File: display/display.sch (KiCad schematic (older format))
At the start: 11 parts

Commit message: More Display work
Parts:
- added C?: 100u, symbol Device:CP
- added C? (x3): 47n, symbol Device:C
- added C?: C, symbol Device:C
- added R?: R, symbol Device:R
- added U? (x2): 74LS139, symbol 74xx_IEEE:74LS139
- added U? (x5): 74LS32, symbol 74xx:74LS32
- added U? (x3): 74HC14, symbol 74xx:74HC14
- added U? (x2): 74LS393, symbol 74xx:74LS393
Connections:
- net labels added: DDg1, DDg2, DDg3, DDg4, ~OE1, ~OE2, ~OE3, ~OE4
- net labels removed: DG1, DG2, DG3, DG4
- wire segments 159 -> 242
- no-connect marks 0 -> 1
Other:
- moved on the sheet: J?, U?, U?A, U?B, U?C

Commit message: lib cache added and display schema
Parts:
- removed RN?: 220x8, symbol Device:R_Pack08
- added C6: 47n, Capacitor_THT:C_Disc_D3.0mm_W1.6mm_P2.50mm, symbol Device:C
- added Q1, Q2, Q3, Q4: 2N3906, Package_TO_SOT_THT:TO-92L_Inline_Wide, symbol Transistor_BJT:2N3906
- added R2, R3, R4, R5: 100, Resistor_THT:R_Axial_DIN0207_L6.3mm_D2.5mm_P7.62mm_Horizontal, symbol Device:R
- added R6: 220, Resistor_THT:R_Axial_DIN0207_L6.3mm_D2.5mm_P7.62mm_Horizontal, symbol Device:R
- added RN1: 220x7, Package_DIP:DIP-14_W7.62mm, symbol Device:R_Pack07
- added U11: 74LS241, Package_DIP:DIP-20_W7.62mm, symbol 74xx:74LS241
- C1: renamed from C?; footprint (none) -> Capacitor_THT:CP_Radial_D6.3mm_P2.50mm
- C2: renamed from C?; value C -> 47n; footprint (none) -> Capacitor_THT:C_Disc_D3.0mm_W1.6mm_P2.50mm
- C3, C4, C5: renamed from C?; footprint (none) -> Capacitor_THT:C_Disc_D3.0mm_W1.6mm_P2.50mm
- J1, J2: renamed from J?; footprint (none) -> Connector_PinHeader_2.54mm:PinHeader_1x24_P2.54mm_Vertical
- R1: renamed from R?; value R -> 47k; footprint (none) -> Resistor_THT:R_Axial_DIN0207_L6.3mm_D2.5mm_P7.62mm_Horizontal
- U1, U3, U4, U5: renamed from U?; footprint (none) -> Package_DIP:DIP-14_W7.62mm
- U2: renamed from U?; footprint (none) -> Package_DIP:DIP-16_W7.62mm
- U6, U7, U8, U9: renamed from U?; footprint (none) -> Package_DIP:DIP-20_W7.62mm
- gave numbers to parts that had none: 1
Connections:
- net labels added: CC1, CC2, CC3, CC4
- wire segments 242 -> 273
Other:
- moved on the sheet: C3, U1G, U3C, U4C, U5E

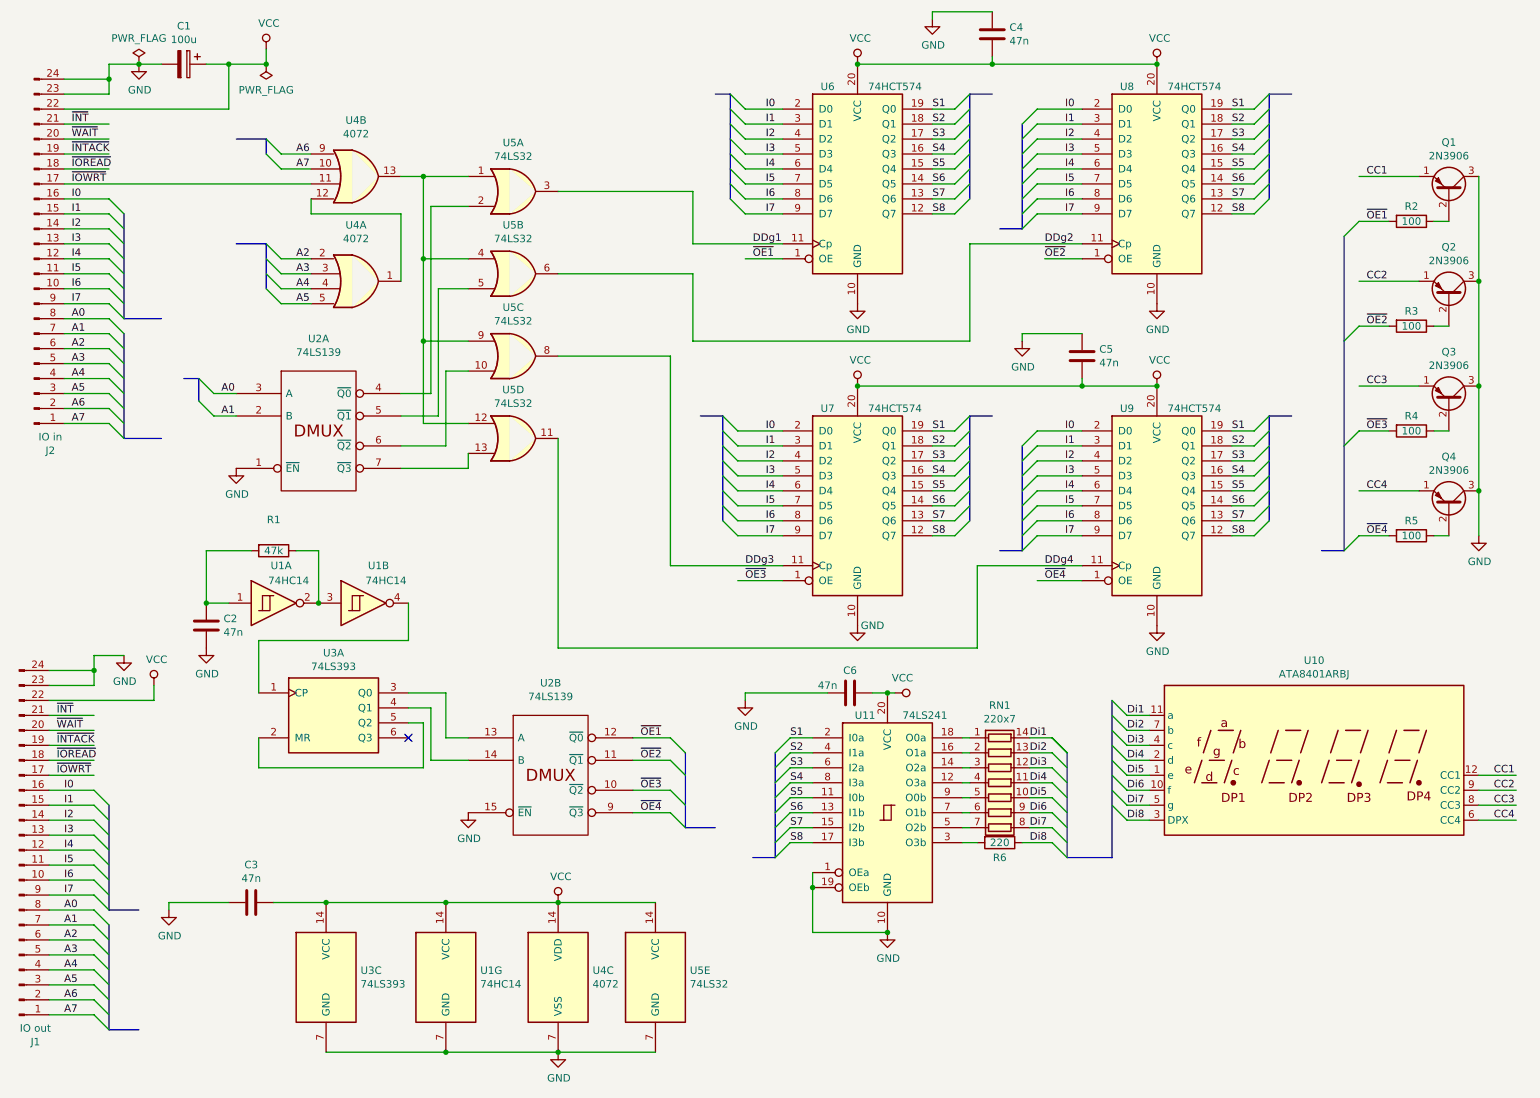
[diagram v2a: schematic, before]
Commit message: display schema first version ready
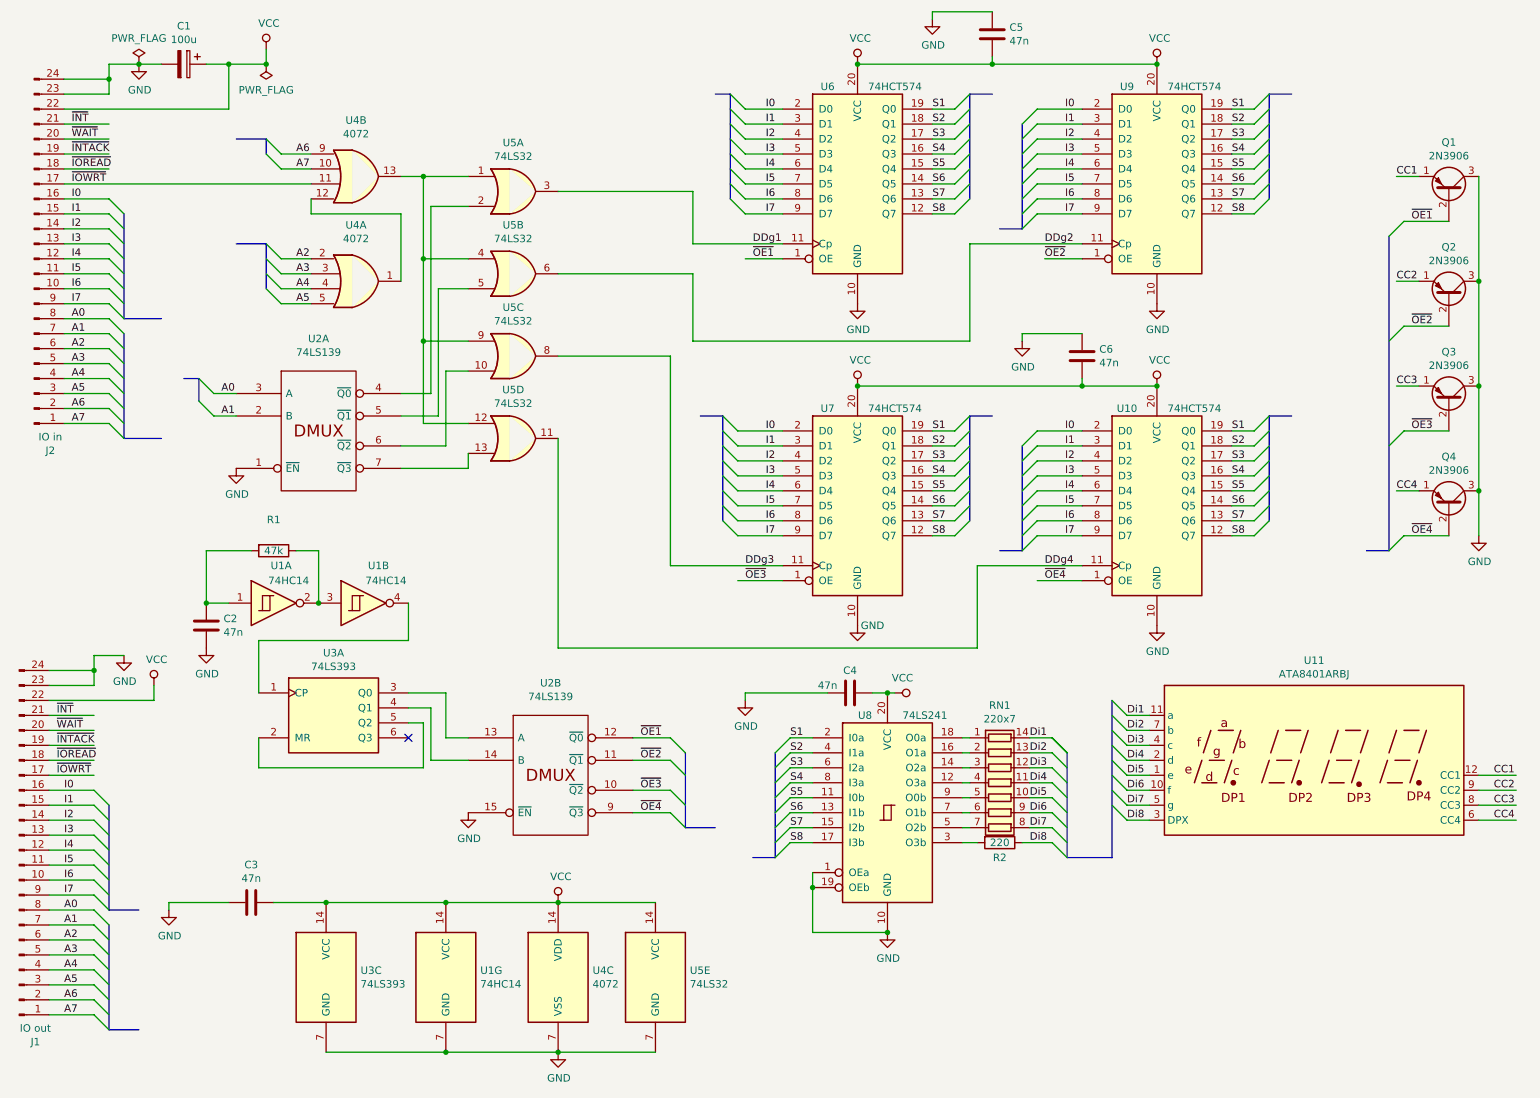
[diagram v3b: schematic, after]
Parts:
- removed R2, R3, R4, R5: 100, Resistor_THT:R_Axial_DIN0207_L6.3mm_D2.5mm_P7.62mm_Horizontal, symbol Device:R
- renumbered C6 to C4, C4 to C5, C5 to C6, R6 to R2, U9 to U10, U10 to U11, U11 to U8, U8 to U9
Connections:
- wire segments 273 -> 269

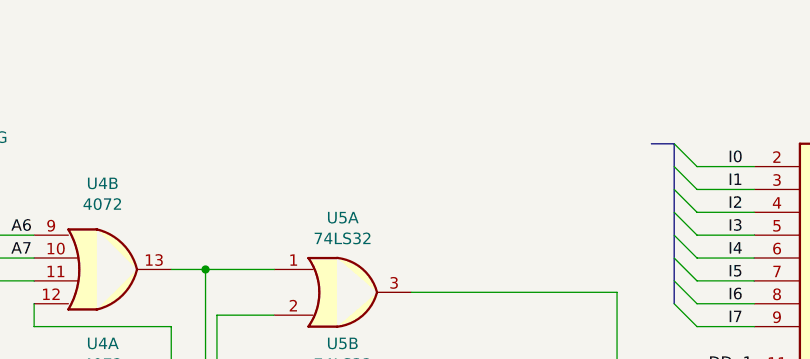
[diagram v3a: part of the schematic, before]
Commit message: display pcb first version ready
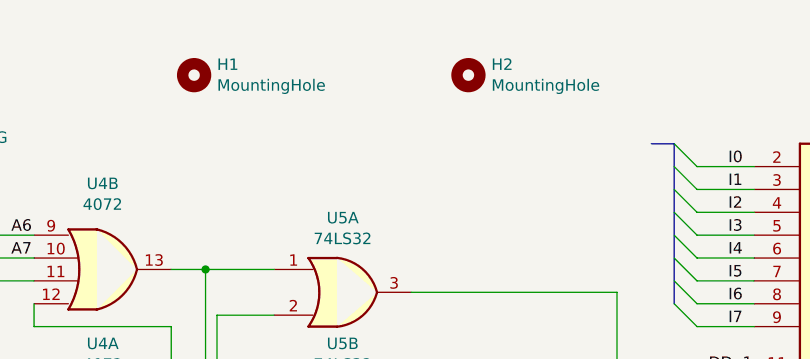
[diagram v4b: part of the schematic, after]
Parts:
- added H1, H2: MountingHole, MountingHole:MountingHole_2.2mm_M2, symbol Mechanical:MountingHole
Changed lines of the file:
@@
 Wire Bus Line
 	8200 5150 8200 6200
+$Comp
+L Mechanical:MountingHole H1
+U 1 1 5DC0A347
+P 3550 800
+F 0 "H1" H 3650 846 50  0000 L CNN
+F 1 "MountingHole" H 3650 755 50  0000 L CNN
+F 2 "MountingHole:MountingHole_2.2mm_M2" H 3550 800 50  0001 C CNN
+F 3 "~" H 3550 800 50  0001 C CNN
+	1    3550 800
+	1    0    0    -1
+$EndComp
+$Comp
+L Mechanical:MountingHole H2
+U 1 1 5DC0A3B3
+P 4750 800
+F 0 "H2" H 4850 846 50  0000 L CNN
+F 1 "MountingHole" H 4850 755 50  0000 L CNN
+F 2 "MountingHole:MountingHole_2.2mm_M2" H 4750 800 50  0001 C CNN
+F 3 "~" H 4750 800 50  0001 C CNN
+	1    4750 800
+	1    0    0    -1
+$EndComp
 $EndSCHEMATC
